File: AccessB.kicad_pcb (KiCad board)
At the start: 2 copper layers, 50 x 50 mm, 30 parts, among them P1 ICSP, P2 USB_OTG, P3 GPIO, P5 USB_OTG, Q1 BSS138, Q2 BSS138, Q3 BSS138, Q4 BSS138, Q5 BSS138, U1 PIC18(L)F2550-I/SO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

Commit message: New update
update
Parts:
- Q1, Q2, Q3, Q4, Q5, R1, R10, R16, R17, R2, R3, R4, R6, R7, R8: moved to F.Cu
- moved Q1 133.9 mm to (169.6, 103.1), turned to 0 degrees
- moved R1 133.7 mm to (169.5, 105.8), turned to 0 degrees
- moved R7 129.5 mm to (169.5, 114.1), turned to 0 degrees
- moved Q4 129.5 mm to (169.6, 111.4), turned to 0 degrees
- moved R3 128.7 mm to (166.9, 103.1)
- moved R10 124.2 mm to (166.9, 111.4)
- moved Q3 111.5 mm to (162.5, 103.1), turned to 0 degrees
- moved R6 111.3 mm to (162.4, 106.1), turned to 0 degrees
- moved R8 105.4 mm to (159.4, 103.2)
- moved Q2 76.5 mm to (117.3, 141.0)
- moved R4 76.3 mm to (120.2, 140.6), turned to 270 degrees
- moved R2 75.6 mm to (117.3, 138.4)
- moved Q5 67.1 mm to (130.2, 128.6), turned to 0 degrees
- moved R16 66.9 mm to (130.1, 131.4), turned to 0 degrees
- moved R17 61.3 mm to (127.3, 129.0)
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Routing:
- net +5V: track 5.84 -> 40.0 mm
- net /GPIO5/RC7: track 12.8 -> 29.3 mm
- net GND: track 0.00 -> 2.55 mm
- net /GPIO4/RC6: track 13.4 -> 15.8 mm

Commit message: update
update
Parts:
- moved R8 35.3 mm to (170.3, 136.8)
- moved R6 32.2 mm to (172.1, 136.8), turned to 90 degrees
- moved Q3 31.3 mm to (171.2, 133.2)
- moved Q4 9.05 mm to (165.8, 103.2)
- moved R7 7.91 mm to (166.7, 106.7), turned to 90 degrees
- moved R2 5.22 mm to (118.7, 143.4), turned to 90 degrees
- moved R10 5.06 mm to (165.0, 106.7)
- moved R4 4.38 mm to (116.9, 143.4), turned to 90 degrees
- moved R3 3.99 mm to (168.7, 106.7)
- moved R17 3.77 mm to (129.3, 132.2)
- moved C4 1.35 mm to (154.0, 100.0), turned to 270 degrees
- moved R1 1.33 mm to (170.5, 106.7), turned to 90 degrees
- moved R16 1.27 mm to (131.1, 132.2), turned to 90 degrees
- moved Q2 1.20 mm to (117.8, 139.9), turned to 0 degrees
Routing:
- net /GPIO5/RC7: track 29.3 -> 20.6 mm, vias 0 -> 2

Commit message: almost end
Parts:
- moved Q2 55.9 mm to (165.8, 111.4)
- moved R2 55.9 mm to (166.7, 115.0)
- moved R4 55.9 mm to (164.9, 115.0)
- moved Q5 43.0 mm to (169.7, 111.4)
- moved R16 43.0 mm to (170.5, 115.0)
- moved R17 43.0 mm to (168.7, 115.0)
- moved R6 31.4 mm to (163.0, 106.8)
- moved R8 31.4 mm to (161.2, 106.8)
- moved Q3 31.4 mm to (162.1, 103.2)
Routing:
- net /GPIO13/RB1: track 12.7 -> 67.2 mm
- net +5V: track 40.0 -> 92.9 mm
- net /GPIO12/RB0: track 14.4 -> 57.7 mm
- net /GPIO11/RA5: track 26.3 -> 60.2 mm
- net /GPIO4/RC6: track 15.8 -> 19.8 mm
- net /GPIO5/RC7: track 20.6 -> 24.6 mm
- net /GPIO12/RB0_VLS: track 0.00 -> 1.68 mm
- net /GPIO11/RA5_VLS: track 0.00 -> 1.67 mm
- net /GPIO13/RB1_VLS: track 0.00 -> 1.65 mm
- net /GPIO5/RC7_VLS: track 0.00 -> 1.64 mm
- net /GPIO4/RC6_VLS: track 0.00 -> 1.61 mm

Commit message: Update
Some reworking....
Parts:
- moved R1 0.10 mm to (170.4, 106.7)
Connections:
- P2 pad 4: Net-(P2-Pad4) -> (no net)
- P3 pad 10: /GPIO11/RA5_VLS -> /GPIO4/RC6_VLS
- P3 pad 2: /GPIO5/RC7_VLS -> /GPIO13/RB1_VLS
- P3 pad 4: /GPIO4/RC6_VLS -> /GPIO11/RA5_VLS
- P3 pad 6: /GPIO13/RB1_VLS -> /GPIO12/RB0_VLS
- P3 pad 8: /GPIO12/RB0_VLS -> /GPIO5/RC7_VLS
- P5 pad 2: Net-(P5-Pad2) -> (no net)
- P5 pad 3: Net-(P5-Pad3) -> (no net)
- P5 pad 4: Net-(P5-Pad4) -> (no net)
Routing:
- net +5V: track 92.9 -> 198.5 mm, vias 0 -> 3
- net /VLS: track 0.00 -> 50.5 mm, vias 0 -> 4
- net /GPIO3/RC2: track 26.7 -> 10.9 mm
- net /GPIO12/RB0_VLS: track 1.68 -> 14.7 mm, vias 0 -> 1
- net /GPIO13/RB1_VLS: track 1.65 -> 11.7 mm, vias 0 -> 1
- net /GPIO11/RA5: track 60.2 -> 50.7 mm
- net /GPIO10/RA4: track 23.7 -> 15.2 mm
- net GND: track 2.55 -> 9.98 mm, vias 0 -> 2
- net /GPIO5/RC7_VLS: track 1.64 -> 8.84 mm, vias 0 -> 1
- net /GPIO4/RC6_VLS: track 1.61 -> 6.91 mm
- net /GPIO11/RA5_VLS: track 1.67 -> 6.05 mm, vias 0 -> 1
- net /GPIO12/RB0: track 57.7 -> 53.5 mm
- net /GPIO2/RC1: track 25.8 -> 23.5 mm
- net /GPIO1/RC0: track 25.3 -> 23.2 mm
- net /GPIO13/RB1: track 67.2 -> 65.8 mm
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
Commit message: more
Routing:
- net /GPIO3/RC2: track 10.9 -> 26.9 mm
- net /GPIO10/RA4: track 15.2 -> 23.9 mm
- net /GPIO12/RB0: track 53.5 -> 60.4 mm
- net /GPIO11/RA5: track 50.7 -> 54.9 mm
- net /GPIO4/RC6_VLS: track 6.91 -> 10.4 mm
- net +5V: track 198.5 -> 201.9 mm
- net /GPIO5/RC7_VLS: track 8.84 -> 11.8 mm
- net /GPIO13/RB1: track 65.8 -> 68.7 mm
- net /GPIO12/RB0_VLS: track 14.7 -> 17.1 mm
- net /GPIO2/RC1: track 23.5 -> 25.8 mm
- net /GPIO1/RC0: track 23.2 -> 25.5 mm

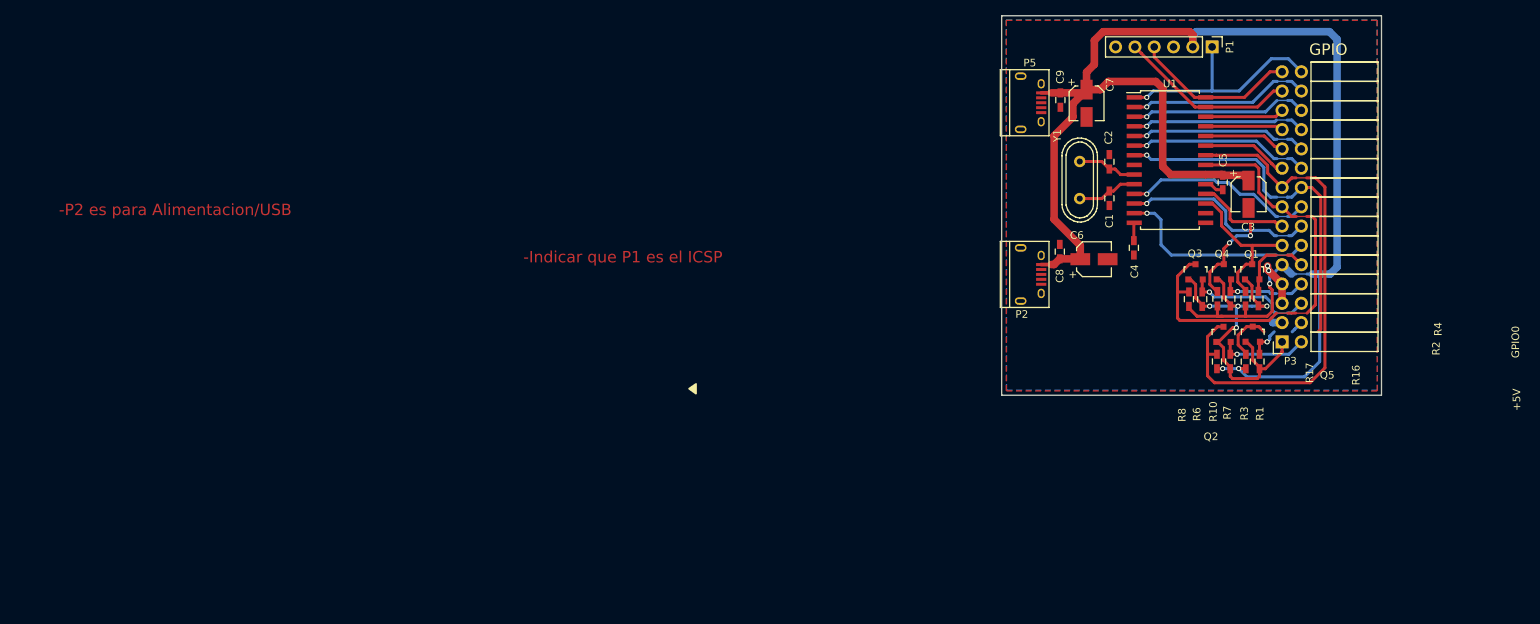
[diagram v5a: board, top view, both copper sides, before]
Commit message: Update
Only need to do routing of USB D+/D- Differential pair.
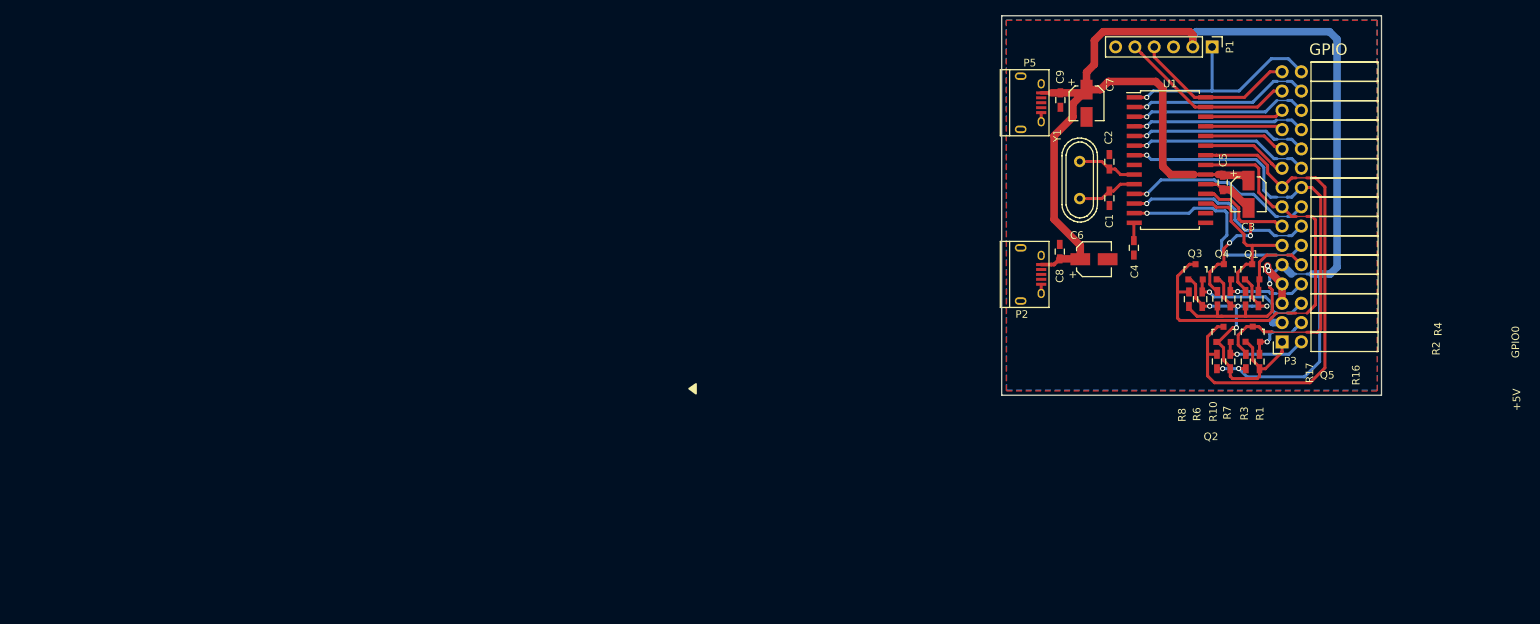
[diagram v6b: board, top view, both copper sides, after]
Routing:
- net GND: track 9.98 -> 18.0 mm
- net /GPIO11/RA5: track 54.9 -> 62.3 mm
- net /GPIO11/RA5_VLS: track 6.05 -> 8.59 mm
- net /GPIO3/RC2: track 26.9 -> 29.4 mm
- net /GPIO4/RC6: track 21.1 -> 22.5 mm
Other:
- board text removed: "-Indicar que P1 es el ICSP"
- board text removed: "-P2 es para Alimentacion/USB"

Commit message: sdf
df
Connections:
- net /D+/RC5 renamed /D+
- net /D-/RC4 renamed /D-

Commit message: more
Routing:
- net /D+: track 0.00 -> 32.8 mm
- net /D-: track 0.00 -> 31.3 mm
- net /GPIO3/RC2: track 29.4 -> 17.7 mm
- net /GPIO5/RC7: track 26.1 -> 25.0 mm
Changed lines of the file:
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@@
     (thickness 1.6)
     (drawings 72)
-    (tracks 488)
+    (tracks 505)
     (zones 0)
     (modules 30)
@@
   (segment (start 174.24 100.95) (end 174.4 100.95) (width 0.1524) (layer B.Cu) (net 11))
   (segment (start 155.725 95.45) (end 161.26 95.45) (width 0.4) (layer B.Cu) (net 11))
-  (segment (start 161.26 95.45) (end 161.92 94.79) (width 0.4) (layer B.Cu) (net 11))
-  (segment (start 161.92 94.79) (end 164.41 94.79) (width 0.4) (layer B.Cu) (net 11))
-  (segment (start 164.41 94.79) (end 164.76 95.14) (width 0.4) (layer B.Cu) (net 11))
-  (segment (start 164.76 95.14) (end 166.02 95.14) (width 0.4) (layer B.Cu) (net 11))
-  (segment (start 166.02 95.14) (end 166.25 95.37) (width 0.4) (layer B.Cu) (net 11))
-  (segment (start 166.25 95.37) (end 166.25 98.34) (width 0.4) (layer B.Cu) (net 11))
-  (segment (start 166.25 98.34) (end 165.56 99.03) (width 0.4) (layer B.Cu) (net 11))
-  (segment (start 165.56 100.26) (end 166.25 100.95) (width 0.4) (layer B.Cu) (net 11))
-  (segment (start 165.56 99.03) (end 165.56 100.26) (width 0.4) (layer B.Cu) (net 11))
   (segment (start 166.25 100.95) (end 172.8 100.95) (width 0.4) (layer B.Cu) (net 11))
   (segment (start 154.05 81.465) (end 155.685 81.465) (width 0.4) (layer F.Cu) (net 12) (status 10))
@@
   (segment (start 169.35 96.55) (end 169.35 98.4) (width 0.4) (layer F.Cu) (net 25))
   (segment (start 169.35 96.55) (end 172.55 96.55) (width 0.4) (layer F.Cu) (net 25))
-  (via (at 166.6 99.35) (size 0.6858) (drill 0.4) (layers F.Cu B.Cu) (net 25))
-  (segment (start 169.35 98.4) (end 167.55 98.4) (width 0.4) (layer B.Cu) (net 25))
-  (segment (start 167.55 98.4) (end 166.6 99.35) (width 0.4) (layer B.Cu) (net 25))
-  (segment (start 166.6 99.35) (end 165.85 100.1) (width 0.4) (layer F.Cu) (net 25))
-  (segment (start 165.85 100.1) (end 165.85 102.15178) (width 0.4) (layer F.Cu) (net 25) (status 20))
   (segment (start 165 105.75) (end 164.93 105.75) (width 0.4) (layer F.Cu) (net 25) (status 30))
   (segment (start 164.93 105.75) (end 164 104.82) (width 0.4) (layer F.Cu) (net 25) (status 10))
@@
   (segment (start 167.81 94.74) (end 167.81 96.194322) (width 0.4) (layer F.Cu) (net 25))
   (segment (start 168.23 96.55) (end 169.35 96.55) (width 0.4) (layer F.Cu) (net 25))
+  (via (at 167.73 100.14) (size 0.6858) (drill 0.4) (layers F.Cu B.Cu) (net 25))
+  (segment (start 165.85 102.15178) (end 165.85 102.02) (width 0.4) (layer F.Cu) (net 25))
+  (segment (start 165.85 102.02) (end 167.73 100.14) (width 0.4) (layer F.Cu) (net 25))
+  (segment (start 167.73 100.02) (end 169.35 98.4) (width 0.4) (layer B.Cu) (net 25))
+  (segment (start 167.73 100.14) (end 167.73 100.02) (width 0.4) (layer B.Cu) (net 25))
   (segment (start 170.54 112.4311) (end 170.600794 112.370306) (width 0.4) (layer F.Cu) (net 26) (status 30))
   (segment (start 170.54 114.02) (end 170.54 112.4311) (width 0.4) (layer F.Cu) (net 26) (status 30))
@@
   (segment (start 179.15241 115.79759) (end 177.18759 117.76241) (width 0.4) (layer F.Cu) (net 31))
   (segment (start 164.61241 117.76241) (end 163.7 116.85) (width 0.4) (layer F.Cu) (net 31))
+  (segment (start 164.56 96.295) (end 165.281832 96.295) (width 0.2) (layer F.Cu) (net 32))
+  (segment (start 163.45 96.705) (end 164.15 96.705) (width 0.2) (layer F.Cu) (net 32))
+  (segment (start 164.15 96.705) (end 164.56 96.295) (width 0.2) (layer F.Cu) (net 32))
+  (segment (start 165.281832 96.295) (end 165.765 96.778168) (width 0.2) (layer F.Cu) (net 32))
+  (segment (start 165.765 96.778168) (end 165.765 98.1468) (width 0.2) (layer F.Cu) (net 32))
+  (segment (start 165.765 98.1468) (end 164.3968 99.515) (width 0.2) (layer F.Cu) (net 32))
+  (segment (start 164.3968 99.515) (end 159.7468 99.515) (width 0.2) (layer F.Cu) (net 32))
+  (segment (start 159.7468 99.515) (end 154.7768 104.485) (width 0.2) (layer F.Cu) (net 32))
+  (segment (start 154.7768 104.485) (end 146.7032 104.485) (width 0.2) (layer F.Cu) (net 32))
+  (segment (start 145.1682 102.95) (end 142.912501 102.95) (width 0.2) (layer F.Cu) (net 32))
+  (segment (start 142.812501 102.85) (end 141.8 102.85) (width 0.2) (layer F.Cu) (net 32))
+  (segment (start 146.7032 104.485) (end 145.1682 102.95) (width 0.2) (layer F.Cu) (net 32))
+  (segment (start 142.912501 102.95) (end 142.812501 102.85) (width 0.2) (layer F.Cu) (net 32))
+  (segment (start 164.56 95.845) (end 165.468232 95.845) (width 0.2) (layer F.Cu) (net 33))
+  (segment (start 164.15 95.435) (end 164.56 95.845) (width 0.2) (layer F.Cu) (net 33))
+  (segment (start 163.45 95.435) (end 164.15 95.435) (width 0.2) (layer F.Cu) (net 33))
+  (segment (start 165.468232 95.845) (end 166.215 96.591768) (width 0.2) (layer F.Cu) (net 33))
+  (segment (start 166.215 96.591768) (end 166.215 98.3332) (width 0.2) (layer F.Cu) (net 33))
+  (segment (start 166.215 98.3332) (end 164.5832 99.965) (width 0.2) (layer F.Cu) (net 33))
+  (segment (start 164.5832 99.965) (end 159.9332 99.965) (width 0.2) (layer F.Cu) (net 33))
+  (segment (start 159.9332 99.965) (end 154.9632 104.935) (width 0.2) (layer F.Cu) (net 33))
+  (segment (start 154.9632 104.935) (end 146.5168 104.935) (width 0.2) (layer F.Cu) (net 33))
+  (segment (start 142.912501 103.4) (end 142.812501 103.5) (width 0.2) (layer F.Cu) (net 33))
+  (segment (start 146.5168 104.935) (end 144.9818 103.4) (width 0.2) (layer F.Cu) (net 33))
+  (segment (start 142.812501 103.5) (end 141.8 103.5) (width 0.2) (layer F.Cu) (net 33))
+  (segment (start 144.9818 103.4) (end 142.912501 103.4) (width 0.2) (layer F.Cu) (net 33))
   (zone (net 2) (net_name GND) (layer F.Cu) (hatch edge 0.508)
     (connect_pads (clearance 0.508))
